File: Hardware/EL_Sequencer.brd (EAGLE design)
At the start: 57.1 x 82.5 mm, 109 parts, among them U1 LM317, U10 Z0103MN, U11 Z0103MN, U12 Z0103MN, U13 MOC3063S, U14 MOC3063S, U15 MOC3063S, U16 MOC3063S, U17 Z0103MN, U18 Z0103MN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

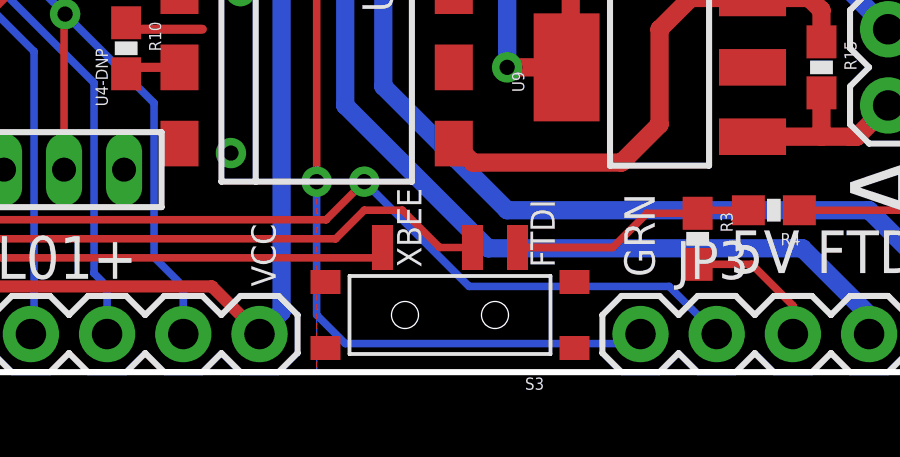
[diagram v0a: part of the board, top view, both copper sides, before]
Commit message: Bumping up drill hits in side smd switch
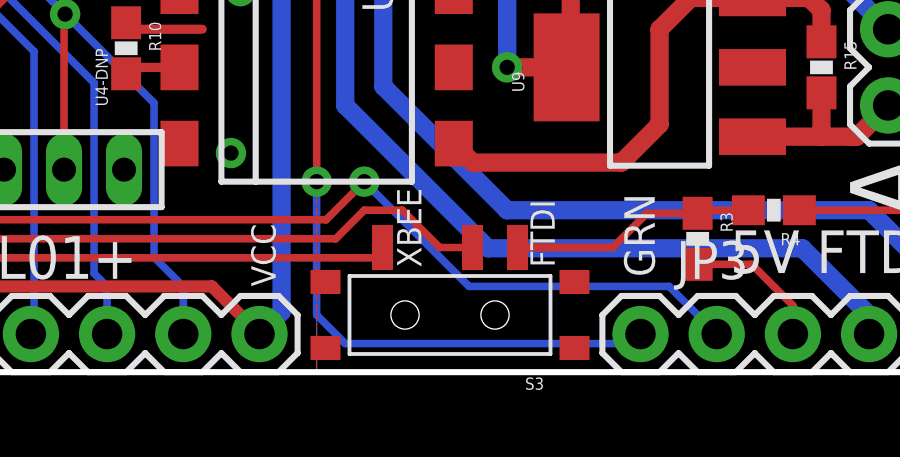
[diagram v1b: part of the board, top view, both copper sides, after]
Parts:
- S3: device SparkFun-Electromechanical:KPS-1290 -> Testing:KPS-1290
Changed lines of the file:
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@@
 <layer number="251" name="SMDround" color="12" fill="11" visible="no" active="no"/>
 <layer number="254" name="cooling" color="7" fill="1" visible="no" active="yes"/>
+<layer number="255" name="routoute" color="7" fill="1" visible="yes" active="yes"/>
 </layers>
 <board>
@@
 <attribute name="PROD_ID" value="DIO-10955" x="18.415" y="50.165" size="1.778" layer="27" font="vector" ratio="15" display="off"/>
 </element>
-<element name="S3" library="SparkFun-Electromechanical" package="KPS-1290" value="SWITCH_SPDT" x="31.115" y="1.905">
+<element name="S3" library="Testing" package="KPS-1290" value="SWITCH_SPDT" x="31.115" y="1.905">
 <attribute name="PROD_ID" value="SWCH-10651" x="31.115" y="1.905" size="1.778" layer="27" font="vector" ratio="15" display="off"/>
 </element>

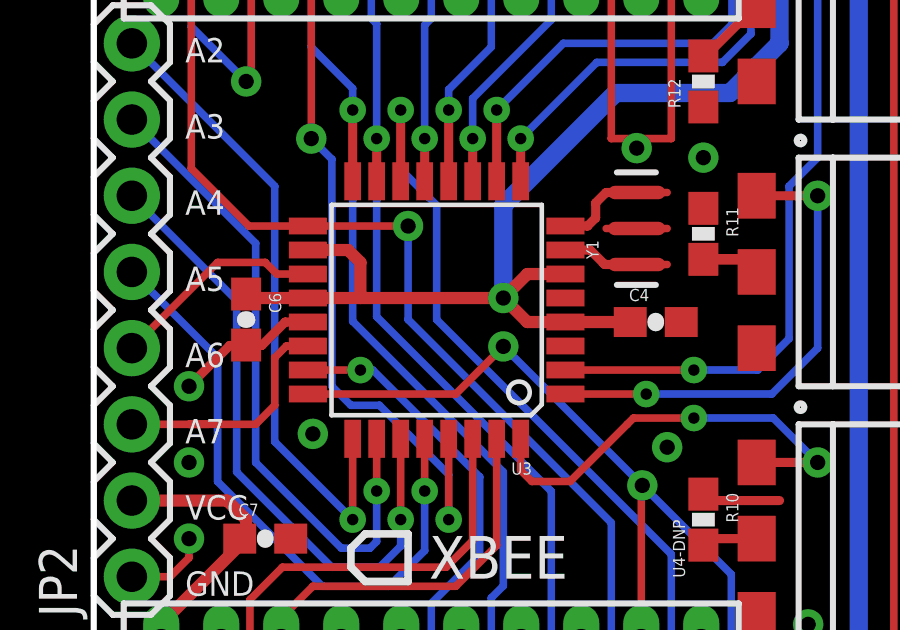
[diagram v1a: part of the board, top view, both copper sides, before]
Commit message: Fixing Redboard errors, updating atmega pkg, deleting tvalue name
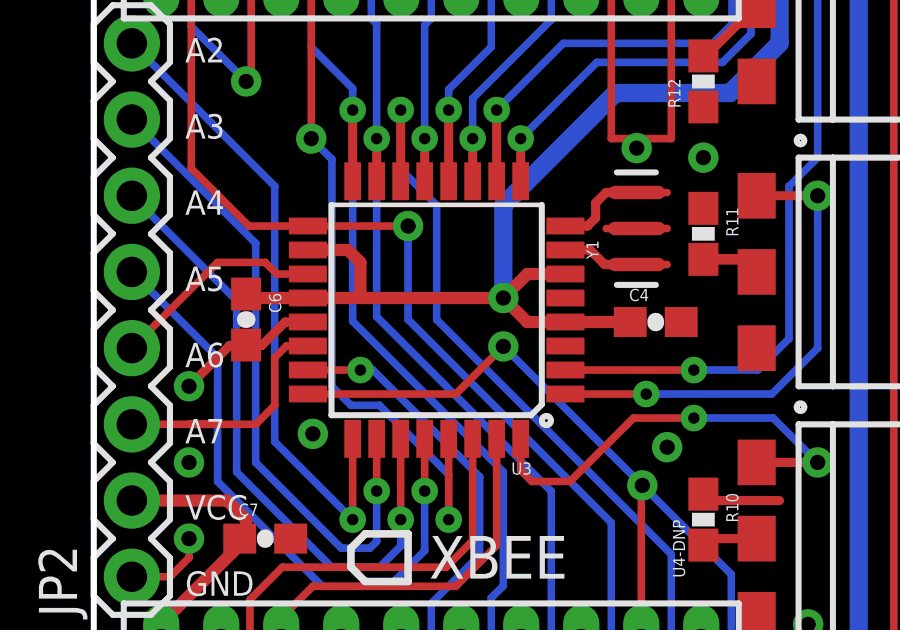
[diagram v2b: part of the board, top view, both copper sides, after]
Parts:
- U3: value ATMEGA328P -> ATMEGA328P_TQFP
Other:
- board text removed: "-M Grusin"
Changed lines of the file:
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@@
 <layer number="47" name="Measures" color="7" fill="1" visible="no" active="yes"/>
 <layer number="48" name="Document" color="7" fill="1" visible="no" active="yes"/>
-<layer number="49" name="Reference" color="7" fill="1" visible="no" active="yes"/>
+<layer number="49" name="Reference" color="7" fill="1" visible="yes" active="yes"/>
 <layer number="50" name="dxf" color="7" fill="1" visible="no" active="yes"/>
 <layer number="51" name="tDocu" color="6" fill="1" visible="yes" active="yes"/>
@@
 <layer number="56" name="wert" color="7" fill="1" visible="no" active="yes"/>
 <layer number="57" name="tCAD" color="7" fill="1" visible="no" active="no"/>
+<layer number="59" name="tCarbon" color="7" fill="1" visible="no" active="no"/>
+<layer number="60" name="bCarbon" color="7" fill="1" visible="no" active="no"/>
 <layer number="90" name="Modules" color="5" fill="1" visible="no" active="no"/>
 <layer number="91" name="Nets" color="2" fill="1" visible="no" active="no"/>
@@
 <layer number="127" name="_tValues" color="7" fill="1" visible="no" active="yes"/>
 <layer number="128" name="_bValues" color="7" fill="1" visible="no" active="yes"/>
+<layer number="129" name="Mask" color="7" fill="1" visible="no" active="yes"/>
 <layer number="131" name="tAdjust" color="7" fill="1" visible="no" active="yes"/>
 <layer number="132" name="bAdjust" color="7" fill="1" visible="no" active="yes"/>
@@
 <layer number="223" name="223bmp" color="24" fill="1" visible="no" active="no"/>
 <layer number="224" name="224bmp" color="25" fill="1" visible="no" active="no"/>
+<layer number="225" name="225bmp" color="7" fill="1" visible="no" active="yes"/>
+<layer number="226" name="226bmp" color="7" fill="1" visible="no" active="yes"/>
+<layer number="227" name="227bmp" color="7" fill="1" visible="no" active="yes"/>
+<layer number="228" name="228bmp" color="7" fill="1" visible="no" active="yes"/>
+<layer number="229" name="229bmp" color="7" fill="1" visible="no" active="yes"/>
+<layer number="230" name="230bmp" color="7" fill="1" visible="no" active="yes"/>
+<layer number="231" name="231bmp" color="7" fill="1" visible="no" active="yes"/>
 <layer number="248" name="Housing" color="7" fill="1" visible="no" active="yes"/>
 <layer number="249" name="Edge" color="7" fill="1" visible="no" active="yes"/>
@@
 <layer number="251" name="SMDround" color="12" fill="11" visible="no" active="no"/>
 <layer number="254" name="cooling" color="7" fill="1" visible="no" active="yes"/>
-<layer number="255" name="routoute" color="7" fill="1" visible="yes" active="yes"/>
+<layer number="255" name="routoute" color="7" fill="1" visible="no" active="yes"/>
 </layers>
 <board>
@@
 <text x="7.9375" y="32.7025" size="0.8128" layer="21" font="vector" ratio="15" rot="SR270">SJ2</text>
 <text x="9.525" y="53.0225" size="1.27" layer="22" font="vector" ratio="15" rot="SMR0">3.5V-16V</text>
-<text x="55.88" y="-22.86" size="1.778" layer="27" font="vector" ratio="10">-M Grusin</text>
 <text x="31.75" y="-13.97" size="1.778" layer="51" font="vector" ratio="15">Nathan Seidle, Mike Grusin</text>
 <text x="31.115" y="-17.78" size="1.778" layer="51" font="vector" ratio="15">Toni Klopfenstein</text>
@@
 <element name="U$6" library="SparkFun-Electromechanical" package="STAND-OFF" value="STAND-OFF" x="2.54" y="80.01"/>
 <element name="U$5" library="SparkFun-Electromechanical" package="STAND-OFF" value="STAND-OFF" x="54.61" y="2.54"/>
-<element name="U3" library="SparkFun-DigitalIC" package="TQFP32-08" value="ATMEGA328P" x="11.43" y="17.78" rot="R180">
+<element name="U3" library="SparkFun-DigitalIC" package="TQFP32-08" value="ATMEGA328P_TQFP" x="11.43" y="17.78" rot="R180">
 <attribute name="PROD_ID" value="IC-09069" x="11.43" y="17.78" size="1.778" layer="27" rot="R180" display="off"/>
-<attribute name="VALUE" value="ATMEGA328P" x="11.43" y="17.78" size="1.778" layer="27" rot="R180" display="off"/>
+<attribute name="VALUE" value="ATMEGA328P_TQFP" x="11.43" y="17.78" size="1.778" layer="27" rot="R180" display="off"/>
 </element>
 <element name="D3" library="SparkFun-LED" package="LED-0603" value="BLUE" x="3.4925" y="33.02">
@@
 <contactref element="D3" pad="C"/>
 <contactref element="JP5" pad="6"/>
-<contactref element="U3" pad="3"/>
-<contactref element="U3" pad="5"/>
 <contactref element="U3" pad="21"/>
 <contactref element="JP3" pad="CTS"/>
@@
 <contactref element="JP1" pad="2"/>
 <contactref element="JP26" pad="1"/>
+<contactref element="U3" pad="3"/>
+<contactref element="U3" pad="5"/>
 </signal>
 <signal name="N$4">
@@
 <signal name="VCC" class="1">
 <contactref element="R8" pad="2"/>
-<contactref element="U3" pad="4"/>
-<contactref element="U3" pad="6"/>
 <contactref element="U3" pad="20"/>
 <contactref element="U3" pad="18"/>
@@
 <wire x1="2.25" y1="6.75" x2="2.25" y2="7.33" width="0.4064" layer="1"/>
 <via x="13.6525" y="18.18" extent="1-16" drill="0.508"/>
-<wire x1="15.7226" y1="17.38" x2="14.4525" y2="17.38" width="0.4064" layer="1"/>
 <wire x1="14.4525" y1="17.38" x2="13.6525" y2="18.18" width="0.4064" layer="1"/>
-<wire x1="15.7226" y1="18.98" x2="14.4525" y2="18.98" width="0.4064" layer="1"/>
 <wire x1="14.4525" y1="18.98" x2="13.6525" y2="18.18" width="0.4064" layer="1"/>
 <wire x1="7.1374" y1="18.18" x2="8.89" y2="18.18" width="0.4064" layer="1"/>
@@
 <wire x1="25.5" y1="41.3225" x2="25.5" y2="31.7975" width="0.6096" layer="16"/>
 <wire x1="25.5" y1="31.7975" x2="25.5" y2="2.005" width="0.6096" layer="16"/>
-<wire x1="15.7226" y1="17.38" x2="17.8825" y2="17.38" width="0.4064" layer="1"/>
 <wire x1="2.25" y1="7.33" x2="5.065" y2="10.145" width="0.4064" layer="1"/>
 <wire x1="2.25" y1="6.75" x2="2.25" y2="6.3225" width="0.4064" layer="1"/>
@@
 <contactref element="C3" pad="A"/>
 <wire x1="5.21" y1="41.91" x2="4.7625" y2="41.91" width="0.254" layer="1"/>
+<contactref element="U3" pad="4"/>
+<contactref element="U3" pad="6"/>
+<wire x1="14.4525" y1="18.98" x2="15.7226" y2="18.98" width="0.4064" layer="1"/>
+<wire x1="14.4525" y1="17.38" x2="15.7226" y2="17.38" width="0.4064" layer="1"/>
+<wire x1="15.7226" y1="17.38" x2="17.8825" y2="17.38" width="0.4064" layer="1"/>
 </signal>
 <signal name="RST">
